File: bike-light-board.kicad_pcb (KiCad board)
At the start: 2 copper layers, 40.2 x 69 mm, 65 parts, among them J1 USB_B_Micro, J2 S2B-PH-SM4-TB, J3 AVR-ISP-6, P1 WirePad, P2 WirePad, P3 WirePad, P4 WirePad, Q1 NCE2003, Q2 NCE2003, Q3 NCE2003, Q4 SMD0805-20, SW1 SW_Push, U1 BRCL4054CME, U2 QMA7981, U3 SSP6206-33NR, U4 ATtiny84A-MU, U5 M74VHC1GT08DFT2G

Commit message: v2
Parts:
- added G***: LOGO, bike-light-board:Logo_Lil_Light, F.Cu at (176.3, 102.3)
- added G***: LOGO, bike-light-board:Logo_Lil_Light, F.Cu at (176.3, 104.9)
- J1: value USB_B_Micro -> USB_Micro_MICRO_4P_DIP; footprint bike-light-board:MICRO-USB-SMD_5PIN-H-FEMALE-PITCH0.65-L_MICRO5.9MMUSB -> footprints:USB_Micro-MICRO_4P_DIP
- moved J1 3.50 mm to (141.0, 103.7), turned to 90 degrees
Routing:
- net GND: track 102.4 -> 101.0 mm, vias 35 -> 34
- net USB_D-: track 14.7 -> 15.7 mm
- net USB_D+: track 9.22 -> 10.2 mm

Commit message: update board
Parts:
- renumbered G*** to LG1, G*** to LG2, G*** to LG3

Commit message: more updates
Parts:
- removed J3: AVR-ISP-6, Connector_PinHeader_2.54mm:PinHeader_2x03_P2.54mm_Vertical_SMD
- removed LG1, LG2: LOGO, bike-light-board:Logo_Lil_Light
- added A1: ANT3216LL00R2400A, footprints:Antenna_3216, F.Cu at (192.0, 106.0)
- added C15: 100n, Capacitor_SMD:C_0402_1005Metric, F.Cu at (209.8, 102.5)
- added C16: C_0402_50V_COG_20p, Capacitor_SMD:C_0402_1005Metric, F.Cu at (215.5, 104.0)
- added C17: C_0402_50V_COG_20p, Capacitor_SMD:C_0402_1005Metric, F.Cu at (219.6, 99.5)
- added C18: 100n, Capacitor_SMD:C_0402_1005Metric, F.Cu at (211.8, 106.4)
- added C19: 100n, Capacitor_SMD:C_0402_1005Metric, F.Cu at (212.7, 104.5)
- added C20: 100n, Capacitor_SMD:C_0402_1005Metric, F.Cu at (219.4, 93.6)
- added C21: 1u, Capacitor_SMD:C_0402_1005Metric, F.Cu at (214.6, 98.1)
- added C22: 100n, Capacitor_SMD:C_0402_1005Metric, F.Cu at (216.5, 93.6)
- added C23: 100n, Capacitor_SMD:C_0402_1005Metric, F.Cu at (216.5, 95.5)
- added C24: C_0402_50V_COG_2p2, Capacitor_SMD:C_0402_1005Metric, F.Cu at (209.0, 106.4)
- added C25: 1u, Capacitor_SMD:C_0402_1005Metric, F.Cu at (216.7, 100.0)
- added C26: C_0402_50V_COG_2p2, Capacitor_SMD:C_0402_1005Metric, F.Cu at (217.4, 97.5)
- added C27: 100n, Capacitor_SMD:C_0402_1005Metric, F.Cu at (212.7, 102.5)
- added C28: DNP, Capacitor_SMD:C_0402_1005Metric, F.Cu at (219.4, 95.5)
- added C29: DNP, Capacitor_SMD:C_0402_1005Metric, F.Cu at (209.8, 104.5)
- added C30: 100n, Capacitor_SMD:C_0402_1005Metric, F.Cu at (213.8, 100.1)
- added C31: 10u, Capacitor_SMD:C_0603_1608Metric, F.Cu at (204.6, 101.0)
- added C32: 10u, Capacitor_SMD:C_0603_1608Metric, F.Cu at (213.5, 89.9)
- added L1: HQ1005C2N0ST, Inductor_SMD:L_0402_1005Metric, F.Cu at (205.8, 98.5)
- added L2: HQ1005C2N0ST, Inductor_SMD:L_0402_1005Metric, F.Cu at (213.6, 96.1)
- added P5: TC2030-IDC-NL_ESP, Connector:Tag-Connect_TC2030-IDC-NL_2x03_P1.27mm_Vertical, F.Cu at (202.3, 91.1)
- added R25: 0R, Resistor_SMD:R_0402_1005Metric, F.Cu at (208.8, 98.5)
- added R26: 0R, Resistor_SMD:R_0402_1005Metric, F.Cu at (217.0, 91.6)
- added R27: 0R, Resistor_SMD:R_0402_1005Metric, F.Cu at (208.0, 100.5)
- added R28: 47k, Resistor_SMD:R_0402_1005Metric, F.Cu at (204.0, 103.2)
- added R29: 47k, Resistor_SMD:R_0402_1005Metric, F.Cu at (217.0, 89.6)
- added U6: M74VHC1GT126DF1G, Package_TO_SOT_SMD:SOT-353_SC-70-5, F.Cu at (206.5, 95.6)
- added Y1: X322540MPB4SI, Crystal:Crystal_SMD_3225-4Pin_3.2x2.5mm, F.Cu at (208.9, 90.8)
- C10, C11, Q1, U2: moved to F.Cu
- C12: value 10n -> 1u; footprint Capacitor_SMD:C_0603_1608Metric -> Capacitor_SMD:C_0402_1005Metric; moved to F.Cu
- C9: value 1u -> 10u; footprint Capacitor_SMD:C_0402_1005Metric -> Capacitor_SMD:C_0603_1608Metric; moved to F.Cu
- R17, R6: value 10k -> 0R; moved to F.Cu
- R19, R20, R21: value 1k5 -> 0R; moved to F.Cu
- R22, R23: value 68 -> 10k; moved to F.Cu
- R3: value 1k5 -> 10k; moved to F.Cu
- R7: value 47k -> 0R; moved to F.Cu
- U3: value SSP6206-33NR -> ESP32-S2; footprint Package_TO_SOT_SMD:SOT-23 -> Package_DFN_QFN:QFN-56-1EP_7x7mm_P0.4mm_EP5.6x5.6mm; moved to F.Cu
- U4: value ATtiny84A-MU -> P25Q40H-SSH-IT; footprint Package_DFN_QFN:QFN-20-1EP_4x4mm_P0.5mm_EP2.6x2.6mm -> Package_SO:SOIC-8_3.9x4.9mm_P1.27mm; moved to F.Cu
- U5: value M74VHC1GT08DFT2G -> ME6231A33PG; footprint Package_TO_SOT_SMD:SOT-353_SC-70-5 -> Package_TO_SOT_SMD:SOT-89-3; moved to F.Cu
- moved R21 64.8 mm to (219.9, 89.6), turned to 0 degrees
- moved R22 61.9 mm to (213.6, 94.1), turned to 0 degrees
- moved R23 60.9 mm to (213.6, 92.1), turned to 0 degrees
- moved C11 59.6 mm to (220.3, 97.5), turned to 0 degrees
- moved R7 59.0 mm to (211.7, 98.1), turned to 0 degrees
- moved C12 53.9 mm to (219.9, 91.6), turned to 0 degrees
- moved R3 51.8 mm to (206.1, 105.2), turned to 0 degrees
- moved R6 50.1 mm to (210.9, 100.5)
- moved U2 49.6 mm to (210.4, 94.8), turned to 0 degrees
- moved R19 49.1 mm to (206.9, 103.2)
- moved C10 46.6 mm to (215.5, 102.0), turned to 0 degrees
- moved U5 44.3 mm to (201.3, 96.7), turned to 0 degrees
- moved R20 40.4 mm to (203.2, 105.2)
- moved Q1 39.0 mm to (200.0, 101.9), turned to 0 degrees
- moved R17 36.1 mm to (200.3, 105.2), turned to 0 degrees
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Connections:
- C11 pad 1: +3V3 -> GND
- C11 pad 2: GND -> +3V3
- C12 pad 1: PROG_nRESET -> +3V3
- C9 pad 1: VSUP -> +3V3
- Q1 pad 1: /VBUS_FET_EN -> (no net)
- Q1 pad 3: /VBUS_FET_EN -> Net-(Q1-Pad3)
- Q1 pad 5: GND -> (no net)
- Q1 pad 6: Net-(Q1-Pad6) -> (no net)
- Q4 pad 2: SW_EN -> LIGHT_SENS_EN
- R1 pad 1: +3V3 -> Net-(C1-Pad1)
- R1 pad 2: Net-(C1-Pad1) -> GND
- R17 pad 1: +3V3 -> /SPI_FL_HD
- R17 pad 2: PROG_nRESET -> Net-(R17-Pad2)
- R18 pad 2: I2C_CLK -> I2C_DATA
- R19 pad 1: PROG_CLK -> /SPI_FL_CLK
- R19 pad 2: I2C_CLK -> Net-(R19-Pad2)
- R20 pad 1: PROG_MOSI -> /SPI_FL_Q
- R20 pad 2: I2C_DATA -> Net-(R20-Pad2)
- R21 pad 1: PROG_MISO -> /SPI_FL_D
- R21 pad 2: BUTTON -> Net-(R21-Pad2)
- R22 pad 1: USB_D+ -> /SPI_FL_CS
- R22 pad 2: /PA0 -> /VDD_SPI
- R23 pad 1: USB_D- -> Net-(R23-Pad1)
- R23 pad 2: /PA1 -> +3V3
- R24 pad 2: I2C_DATA -> I2C_CLK
- R3 pad 1: +3V3 -> /nRESET
- R3 pad 2: USB_D- -> +3V3
- R6 pad 1: CHRG_STAT -> Net-(C16-Pad1)
- R6 pad 2: Net-(Q1-Pad6) -> Net-(R6-Pad2)
- R7 pad 1: VBUS -> /SPI_FL_WP
- R7 pad 2: GND -> Net-(R7-Pad2)
- R8 pad 1: /VBUS_FET_EN -> Net-(Q1-Pad3)
- SW1 pad 1: Net-(C1-Pad1) -> +3V3
- SW1 pad 2: GND -> Net-(C1-Pad1)
- U2 pad 10: (no net) -> +3V3
- U3 pad 1: GND -> +3V3
- U3 pad 2: +3V3 -> /RF_LNA
- U3 pad 3: VSUP -> Net-(C19-Pad2)
- U4 pad 1: I2C_CLK -> /SPI_FL_CS
- U4 pad 2: LIGHT_SENS -> /SPI_FL_Q
- U4 pad 3: CHRG_STAT -> /SPI_FL_WP
- U4 pad 4: /PA1 -> GND
- U4 pad 5: /PA0 -> /SPI_FL_D
- U4 pad 6: (no net) -> /SPI_FL_CLK
- U4 pad 7: (no net) -> /SPI_FL_HD
- U4 pad 8: GND -> /VDD_SPI
- U5 pad 1: LED_DATA -> GND
- U5 pad 2: LED_DATA -> VSUP
- U5 pad 3: GND -> +3V3
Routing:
- net Net-(Q1-Pad3): track 0.00 -> 9.69 mm, vias 0 -> 1
- net /VBUS_FET_EN: track 9.69 -> 0.00 mm, vias 1 -> 0
- net Net-(C1-Pad1): track 17.7 -> 25.8 mm, vias 0 -> 1
- net GND: track 101.0 -> 93.0 mm, vias 34 -> 33
- net I2C_DATA: track 7.28 -> 8.62 mm
- net I2C_CLK: track 8.62 -> 7.28 mm

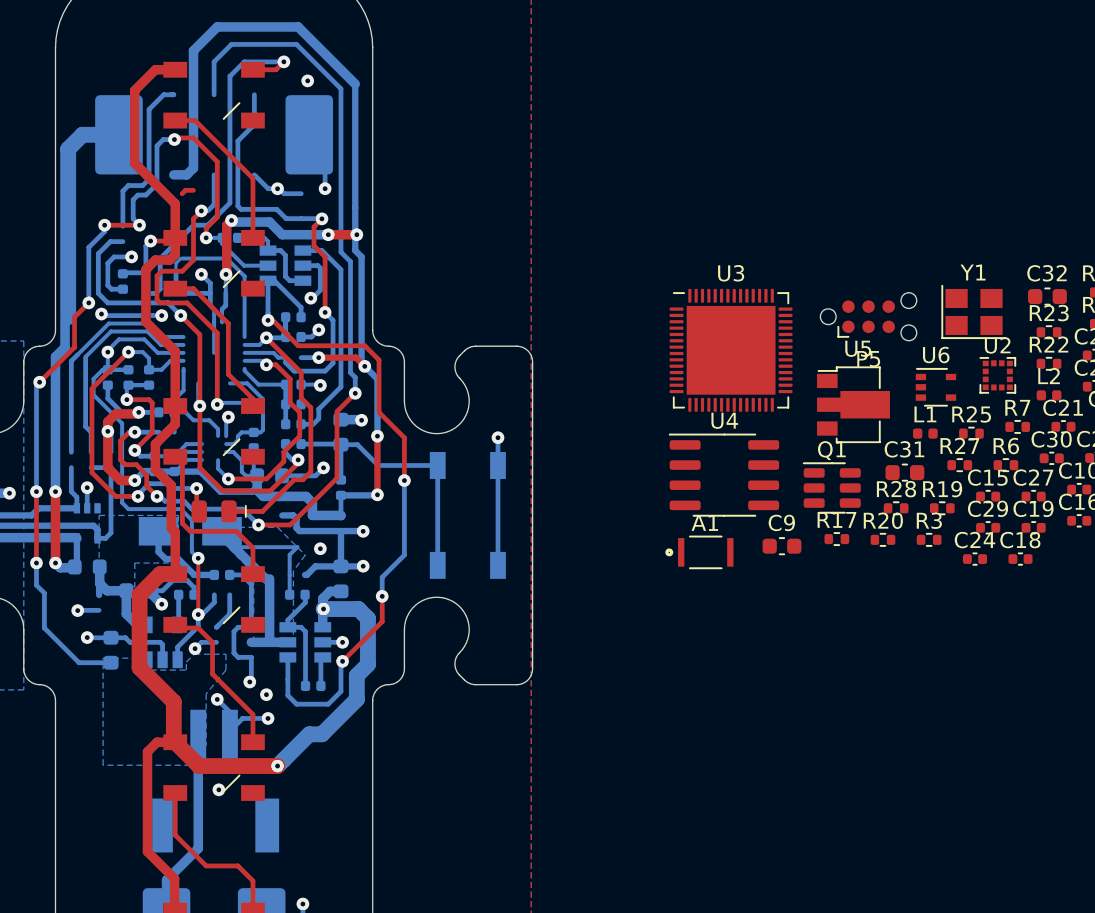
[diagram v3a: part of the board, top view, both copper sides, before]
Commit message: clean up schematic
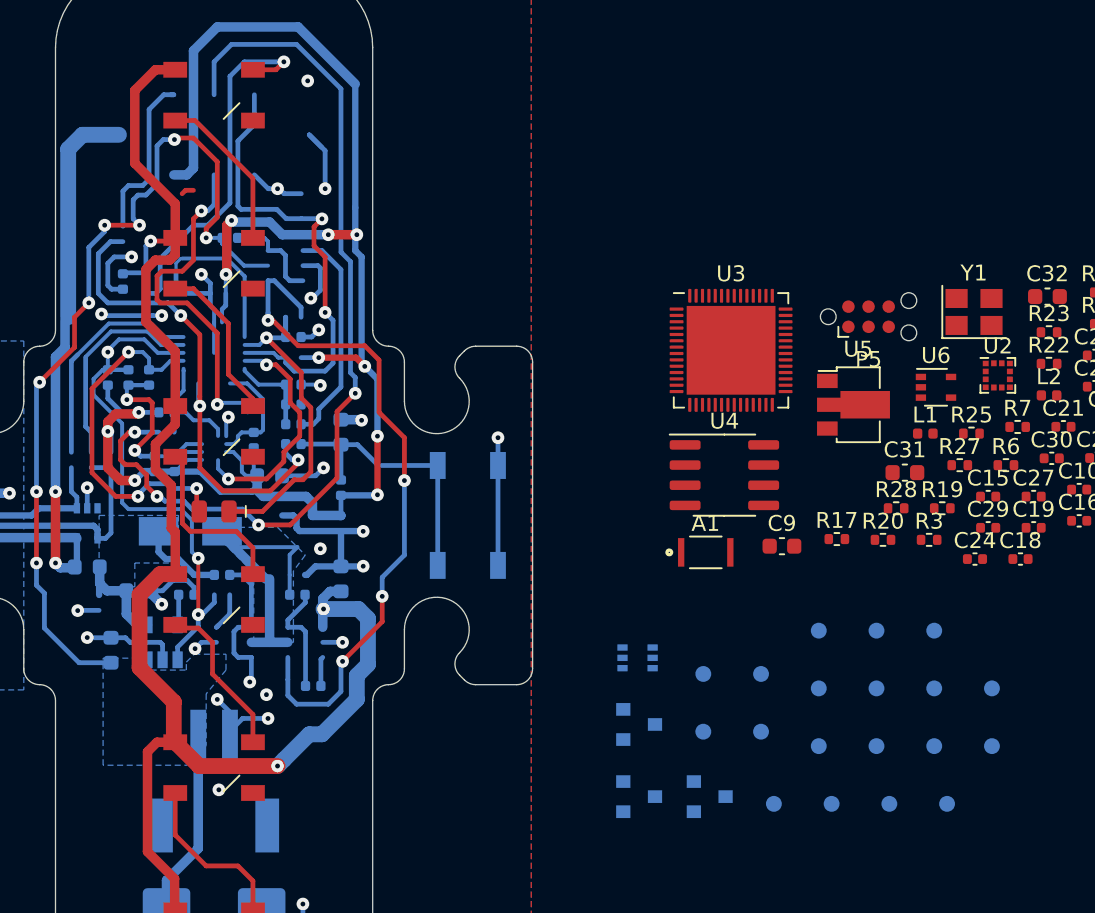
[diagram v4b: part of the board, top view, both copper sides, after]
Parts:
- removed P1, P4: WirePad, bike-light-board:Solder_Wire_Pad_5mmx3mm
- removed R15: 68, Resistor_SMD:R_0402_1005Metric
- added Q5: HX2301A, Package_TO_SOT_SMD:SOT-23, B.Cu at (192.2, 121.4)
- added TP1: TestPoint_ICT_1mm, footprints:ICT_TestPoint_Pad_D1.00mm, B.Cu at (196.3, 121.9)
- added TP10: TestPoint_ICT_1mm, footprints:ICT_TestPoint_Pad_D1.00mm, B.Cu at (199.1, 114.6)
- added TP11: TestPoint_ICT_1mm, footprints:ICT_TestPoint_Pad_D1.00mm, B.Cu at (207.2, 121.9)
- added TP12: TestPoint_ICT_1mm, footprints:ICT_TestPoint_Pad_D1.00mm, B.Cu at (202.8, 114.6)
- added TP13: TestPoint_ICT_1mm, footprints:ICT_TestPoint_Pad_D1.00mm, B.Cu at (206.4, 118.2)
- added TP14: TestPoint_ICT_1mm, footprints:ICT_TestPoint_Pad_D1.00mm, B.Cu at (199.1, 110.9)
- added TP15: TestPoint_ICT_1mm, footprints:ICT_TestPoint_Pad_D1.00mm, B.Cu at (202.8, 110.9)
- added TP16: TestPoint_ICT_1mm, footprints:ICT_TestPoint_Pad_D1.00mm, B.Cu at (206.4, 114.6)
- added TP17: TestPoint_ICT_1mm, footprints:ICT_TestPoint_Pad_D1.00mm, B.Cu at (210.0, 118.2)
- added TP18: TestPoint_ICT_1mm, footprints:ICT_TestPoint_Pad_D1.00mm, B.Cu at (206.4, 110.9)
- added TP19: TestPoint_ICT_1mm, footprints:ICT_TestPoint_Pad_D1.00mm, B.Cu at (210.0, 114.6)
- added TP2: TestPoint_ICT_1mm, footprints:ICT_TestPoint_Pad_D1.00mm, B.Cu at (191.8, 117.3)
- added TP3: TestPoint_ICT_1mm, footprints:ICT_TestPoint_Pad_D1.00mm, B.Cu at (195.5, 117.3)
- added TP4: TestPoint_ICT_1mm, footprints:ICT_TestPoint_Pad_D1.00mm, B.Cu at (191.8, 113.7)
- added TP5: TestPoint_ICT_1mm, footprints:ICT_TestPoint_Pad_D1.00mm, B.Cu at (199.9, 121.9)
- added TP6: TestPoint_ICT_1mm, footprints:ICT_TestPoint_Pad_D1.00mm, B.Cu at (195.5, 113.7)
- added TP7: TestPoint_ICT_1mm, footprints:ICT_TestPoint_Pad_D1.00mm, B.Cu at (203.6, 121.9)
- added TP8: TestPoint_ICT_1mm, footprints:ICT_TestPoint_Pad_D1.00mm, B.Cu at (199.1, 118.2)
- added TP9: TestPoint_ICT_1mm, footprints:ICT_TestPoint_Pad_D1.00mm, B.Cu at (202.8, 118.2)
- Q1: value NCE2003 -> HX2301A; footprint Package_TO_SOT_SMD:SOT-23-6 -> Package_TO_SOT_SMD:SOT-23; moved to B.Cu
- Q2: value NCE2003 -> L2N7002DW1T1G; footprint Package_TO_SOT_SMD:SOT-23-6 -> Package_TO_SOT_SMD:SOT-363_SC-70-6
- Q3: value NCE2003 -> HX2301A; footprint Package_TO_SOT_SMD:SOT-23-6 -> Package_TO_SOT_SMD:SOT-23
- R14: value 10k -> 47k
- moved Q3 36.5 mm to (187.8, 116.8)
- moved Q1 23.0 mm to (187.8, 121.4)
- moved Q2 21.0 mm to (187.7, 112.7)
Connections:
- C28 pad 1: USB_D- -> Net-(C28-Pad1)
- C29 pad 1: USB_D+ -> Net-(C29-Pad1)
- D1 pad 1: USB_D+ -> Net-(C28-Pad1)
- D1 pad 4: USB_D- -> Net-(C29-Pad1)
- J1 pad 2: USB_D- -> Net-(C29-Pad1)
- J1 pad 3: USB_D+ -> Net-(C28-Pad1)
- Q1 pad 1: (no net) -> Net-(Q1-Pad1)
- Q1 pad 3: Net-(Q1-Pad3) -> +BATT
- Q2 pad 1: /SW_FET_EN -> GND
- Q2 pad 2: VSUP -> SW_EN
- Q2 pad 4: +VSW -> GND
- Q2 pad 5: GND -> SW_EN
- Q3 pad 1: /SW_FET_EN -> Net-(Q2-Pad3)
- R10 pad 2: Net-(Q3-Pad3) -> Net-(Q2-Pad3)
- R11 pad 1: Net-(Q2-Pad3) -> Net-(Q5-Pad1)
- R12 pad 1: Net-(Q3-Pad4) -> Net-(Q3-Pad3)
- R25 pad 1: Net-(R25-Pad1) -> USB_D+
- R25 pad 2: USB_D- -> Net-(C28-Pad1)
- R26 pad 1: Net-(R26-Pad1) -> USB_D-
- R26 pad 2: USB_D+ -> Net-(C29-Pad1)
- R8 pad 1: Net-(Q1-Pad3) -> Net-(Q1-Pad1)
- R9 pad 2: Net-(Q2-Pad3) -> Net-(Q5-Pad1)
- U3 pad 25: Net-(R25-Pad1) -> USB_D-
- U3 pad 26: Net-(R26-Pad1) -> USB_D+
- U3 pad 43: (no net) -> Net-(TP1-Pad1)
- U3 pad 44: (no net) -> Net-(TP2-Pad1)
- U3 pad 46: (no net) -> Net-(TP3-Pad1)
- U3 pad 47: (no net) -> Net-(TP4-Pad1)
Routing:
- net USB_D-: track 15.7 -> 0.00 mm
- net Net-(C29-Pad1): track 0.00 -> 15.7 mm
- net Net-(Q3-Pad4): track 14.1 -> 0.00 mm
- net USB_D+: track 10.2 -> 0.00 mm
- net Net-(C28-Pad1): track 0.00 -> 10.2 mm
- net Net-(Q1-Pad3): track 9.69 -> 0.00 mm, vias 1 -> 0
- net Net-(Q1-Pad1): track 0.00 -> 9.69 mm, vias 0 -> 1
- net Net-(Q3-Pad3): track 6.35 -> 14.1 mm
- net Net-(Q5-Pad1): track 0.00 -> 7.17 mm
- net GND: track 93.0 -> 89.1 mm, vias 33 -> 31
- net (no net): track 0.00 -> 3.84 mm, vias 0 -> 2
- net Net-(Q2-Pad3): track 7.17 -> 6.35 mm

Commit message: placement
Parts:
- removed P5: TC2030-IDC-NL_ESP, Connector:Tag-Connect_TC2030-IDC-NL_2x03_P1.27mm_Vertical
- removed R21: 0R, Resistor_SMD:R_0402_1005Metric
- removed TP1, TP15, TP16, TP2, TP3, TP4: TestPoint_ICT_1mm, footprints:ICT_TestPoint_Pad_D1.00mm
- added C33: 10n, Capacitor_SMD:C_0603_1608Metric, B.Cu at (169.8, 106.5)
- added R15: 2k, Resistor_SMD:R_0402_1005Metric, B.Cu at (167.7, 99.9)
- added SW2: STO-060A16AB, footprints:STO-060A16AB, B.Cu at (179.0, 96.7)
- added SW3: STO-060A16AB, footprints:STO-060A16AB, B.Cu at (179.0, 110.7)
- A1, C10, C11, C15, C16, C17, C18, C19, C20, C21, C22, C23, C24, C25, C26, C27, C28, C29, C30, C31, C32, C9, L1, L2, R23, R25, R26, R27, R28, R29, R3, R6, R7, U2, U4, U5, U6, Y1: moved to B.Cu
- C12: value 1u -> 10n; footprint Capacitor_SMD:C_0402_1005Metric -> Capacitor_SMD:C_0603_1608Metric; moved to B.Cu
- J1: value USB_Micro_MICRO_4P_DIP -> KH-TYPE-C-16P; footprint footprints:USB_Micro-MICRO_4P_DIP -> footprints:USB_C_Receptacle_KH-TYPE-C-16P
- R17: value 0R -> 2k; moved to B.Cu
- R19, R20: value 0R -> 5k1; moved to B.Cu
- R22: value 10k -> DNP; moved to B.Cu
- U3: footprint Package_DFN_QFN:QFN-56-1EP_7x7mm_P0.4mm_EP5.6x5.6mm -> footprints:ESP32-S2; moved to B.Cu
- moved C17 65.4 mm to (154.3, 94.8)
- moved TP13 64.0 mm to (142.8, 125.2)
- moved TP19 63.5 mm to (146.8, 120.0)
- moved C16 62.3 mm to (155.0, 89.4), turned to 180 degrees
- moved C23 59.0 mm to (157.5, 94.4), turned to 180 degrees
- moved C26 58.9 mm to (160.0, 84.3), turned to 180 degrees
- moved C11 58.7 mm to (162.8, 85.5), turned to 180 degrees
- moved C21 58.0 mm to (157.5, 87.7), turned to 180 degrees
- moved C18 56.1 mm to (157.5, 92.7), turned to 180 degrees
- moved C10 55.6 mm to (163.0, 84.0)
- moved TP11 55.0 mm to (158.0, 97.3)
- moved R19 54.9 mm to (152.0, 101.5), turned to 90 degrees
- moved Y1 54.3 mm to (154.7, 92.1), turned to 270 degrees
- moved R6 54.2 mm to (157.5, 91.2)
- moved C32 54.2 mm to (163.2, 110.0), turned to 90 degrees
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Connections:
- net +BATT renamed /VBAT
- net VSUP renamed /VSUP
- C12 pad 1: +3V3 -> Net-(C12-Pad1)
- C21 pad 1: /nRESET -> EN
- C28 pad 1: Net-(C28-Pad1) -> /USB+
- C29 pad 1: Net-(C29-Pad1) -> /USB-
- C3 pad 1: VBUS -> /VBUS
- C4 pad 1: CHRG_STAT -> +3V3
- C8 pad 1: BATT_MONITOR -> VBAT_MONITOR
- D1 pad 1: Net-(C28-Pad1) -> (no net)
- D1 pad 3: (no net) -> /VBUS_IN
- D1 pad 4: Net-(C29-Pad1) -> /USB-
- D1 pad 5: Net-(D1-Pad5) -> /USB+
- D2 pad 2: VBUS -> /VBUS
- F1 pad 1: VBUS -> /VBUS
- F1 pad 2: Net-(D1-Pad5) -> /VBUS_IN
- R12 pad 2: BATT_MONITOR -> VBAT_MONITOR
- R13 pad 1: BATT_MONITOR -> VBAT_MONITOR
- R17 pad 1: /SPI_FL_HD -> Net-(C33-Pad1)
- R17 pad 2: Net-(R17-Pad2) -> EN
- R19 pad 1: /SPI_FL_CLK -> Net-(J1-PadB5)
- R19 pad 2: Net-(R19-Pad2) -> GND
- R20 pad 1: /SPI_FL_Q -> Net-(J1-PadA5)
- R20 pad 2: Net-(R20-Pad2) -> GND
- R25 pad 2: Net-(C28-Pad1) -> /USB+
- R26 pad 2: Net-(C29-Pad1) -> /USB-
- R28 pad 1: VBUS -> /VBUS
- R3 pad 1: /nRESET -> EN
- R4 pad 1: Net-(R4-Pad1) -> CHRG_I_MONITOR
- R7 pad 1: /SPI_FL_WP -> Net-(R7-Pad1)
- R7 pad 2: Net-(R7-Pad2) -> /SPI_FL_CLK
- R8 pad 1: Net-(Q1-Pad1) -> /VBUS
- R8 pad 2: VBUS -> Net-(Q1-Pad1)
- TP12 pad 1: /nRESET -> Net-(C33-Pad1)
- TP13 pad 1: /BT -> CHRG_STAT
- TP14 pad 1: GND -> Net-(C12-Pad1)
- TP6 pad 1: Net-(C28-Pad1) -> /USB+
- TP7 pad 1: Net-(C29-Pad1) -> /USB-
- TP9 pad 1: Net-(D1-Pad5) -> /VBUS_IN
- U1 pad 4: VBUS -> /VBUS
- U1 pad 5: Net-(R4-Pad1) -> CHRG_I_MONITOR
- U3 pad 10: BUTTON -> ACCEL_INT
- U3 pad 11: ACCEL_INT -> VBUS_MONITOR
- U3 pad 12: LIGHT_SENS_EN -> VBAT_MONITOR
- U3 pad 13: (no net) -> LIGHT_SENS
- U3 pad 14: (no net) -> CHRG_STAT
- U3 pad 15: (no net) -> CHRG_I_MONITOR
- U3 pad 16: (no net) -> LED_DATA
- U3 pad 23: Net-(R23-Pad1) -> BUTTON
- U3 pad 24: (no net) -> Net-(R23-Pad1)
- U3 pad 31: Net-(R17-Pad2) -> /SPI_FL_HD
- U3 pad 32: Net-(R7-Pad2) -> /SPI_FL_WP
- U3 pad 34: Net-(R19-Pad2) -> Net-(R7-Pad1)
- U3 pad 35: Net-(R20-Pad2) -> /SPI_FL_Q
- U3 pad 36: Net-(R21-Pad2) -> /SPI_FL_D
- U3 pad 39: LED_DATA -> (no net)
- U3 pad 41: SW_EN -> LIGHT_SENS_EN
- U3 pad 42: (no net) -> SW_EN
- U3 pad 43: Net-(TP1-Pad1) -> (no net)
- U3 pad 44: Net-(TP2-Pad1) -> (no net)
- U3 pad 46: Net-(TP3-Pad1) -> (no net)
- U3 pad 47: Net-(TP4-Pad1) -> (no net)
- U3 pad 5: /BT -> IO0
- U3 pad 56: /nRESET -> EN
- U3 pad 6: VBUS_MONITOR -> (no net)
- U3 pad 7: BATT_MONITOR -> (no net)
- U3 pad 8: LIGHT_SENS -> (no net)
- U3 pad 9: CHRG_STAT -> (no net)
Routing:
- net +VSW: track 94.8 -> 4.93 mm, vias 3 -> 4
- net +3V3: track 106.3 -> 40.8 mm
- net PROG_CLK: track 57.9 -> 0.00 mm, vias 4 -> 0
- net /VBAT: track 68.2 -> 11.1 mm, vias 8 -> 0
- net GND: track 89.1 -> 44.0 mm, vias 31 -> 65
- net /SW_FET_EN: track 44.0 -> 0.00 mm, vias 4 -> 0
- net Net-(D1-Pad5): track 39.8 -> 0.00 mm, vias 2 -> 0
- net /USB-: track 0.00 -> 39.5 mm
- net /USB+: track 0.00 -> 37.2 mm
- net CHRG_STAT: track 35.1 -> 5.10 mm, vias 3 -> 2
- net PROG_nRESET: track 29.6 -> 0.00 mm, vias 2 -> 0
- net BUTTON: track 31.1 -> 3.26 mm, vias 3 -> 0
- net Net-(D3-Pad4): track 22.7 -> 0.00 mm, vias 1 -> 0
- net PROG_MOSI: track 21.6 -> 0.00 mm, vias 2 -> 0
- net SW_EN: track 20.8 -> 3.21 mm
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- added copper zone on B.Cu, net /VBUS_IN
- added copper zone on In2.Cu, net GND
- removed copper zone on B.Cu, net /VBAT
- removed copper zone on F.Cu, net GND
- removed copper zone on B.Cu, net Net-(J1-Pad6)
- removed copper zone on B.Cu, net VBUS
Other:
- outline, holes or cut-outs redrawn
- copper layers 2 -> 4
- net class Default: clearance 0.2 -> 0.127; trace_width 0.25 -> 0.13; via_dia 0.8 -> 0.5; via_drill 0.3 -> 0.2
- net class RF added: clearance 0.127, trace_width 0.29, via_dia 0.5, via_drill 0.2
- net class USB added: clearance 0.127, trace_width 0.13, via_dia 0.5, via_drill 0.2
- rule trace_clearance: 0.2 -> 0.127
- rule trace_min: 0.2 -> 0.13
- rule via_min_drill: 0.3 -> 0.2
- rule via_min_size: 0.4 -> 0.5
- board text added: "50 ohm - 0.29 mm"
- board text added: "BOTTOM- Signal"
- board text added: "Layer 2- Power plane"
- board text added: "Layer 3- Solid GND plane"
- board text added: "STACKUP: JLC7628"
- board text added: "TOP- power, signal"
- board text removed: "1"
- board text removed: "5V IN"
